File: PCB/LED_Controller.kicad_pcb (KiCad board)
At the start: 2 copper layers, 89.5 x 60.5 mm, 87 parts, among them J1 Barrel_Jack, J2 Conn_01x06_Female, J3 74984104400, J4 Screw_Terminal_01x02, J5 Screw_Terminal_01x04, Q1 MMBF170, U1 ESP32-PICO-D4, U2 AP62200WU-7, U3 TPS2372, U4 74LVCH2T45DC, U5 LAN8720A, U6 MCP1792x-5002xCB, U7 VCB4805SBO-50WR3, Y1 ECS-250-20-33-CKM-TR

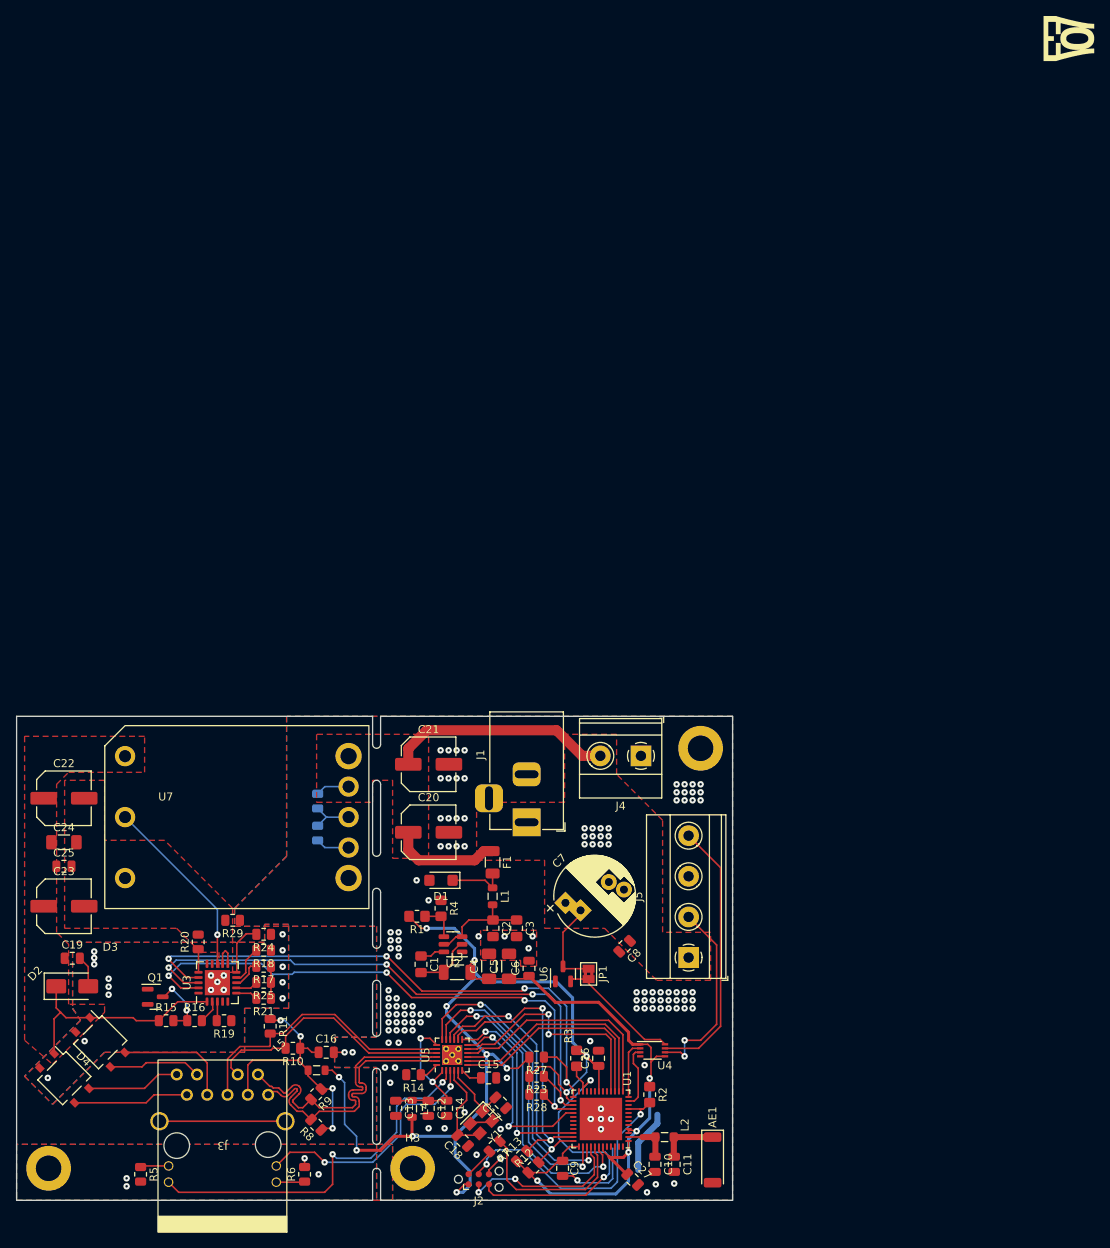
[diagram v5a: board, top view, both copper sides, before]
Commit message: Almost-Almost PCB design. Minor improvements on copper layer Silkscreen cleanup schematic sheet cleanup (now with subsheet titles)
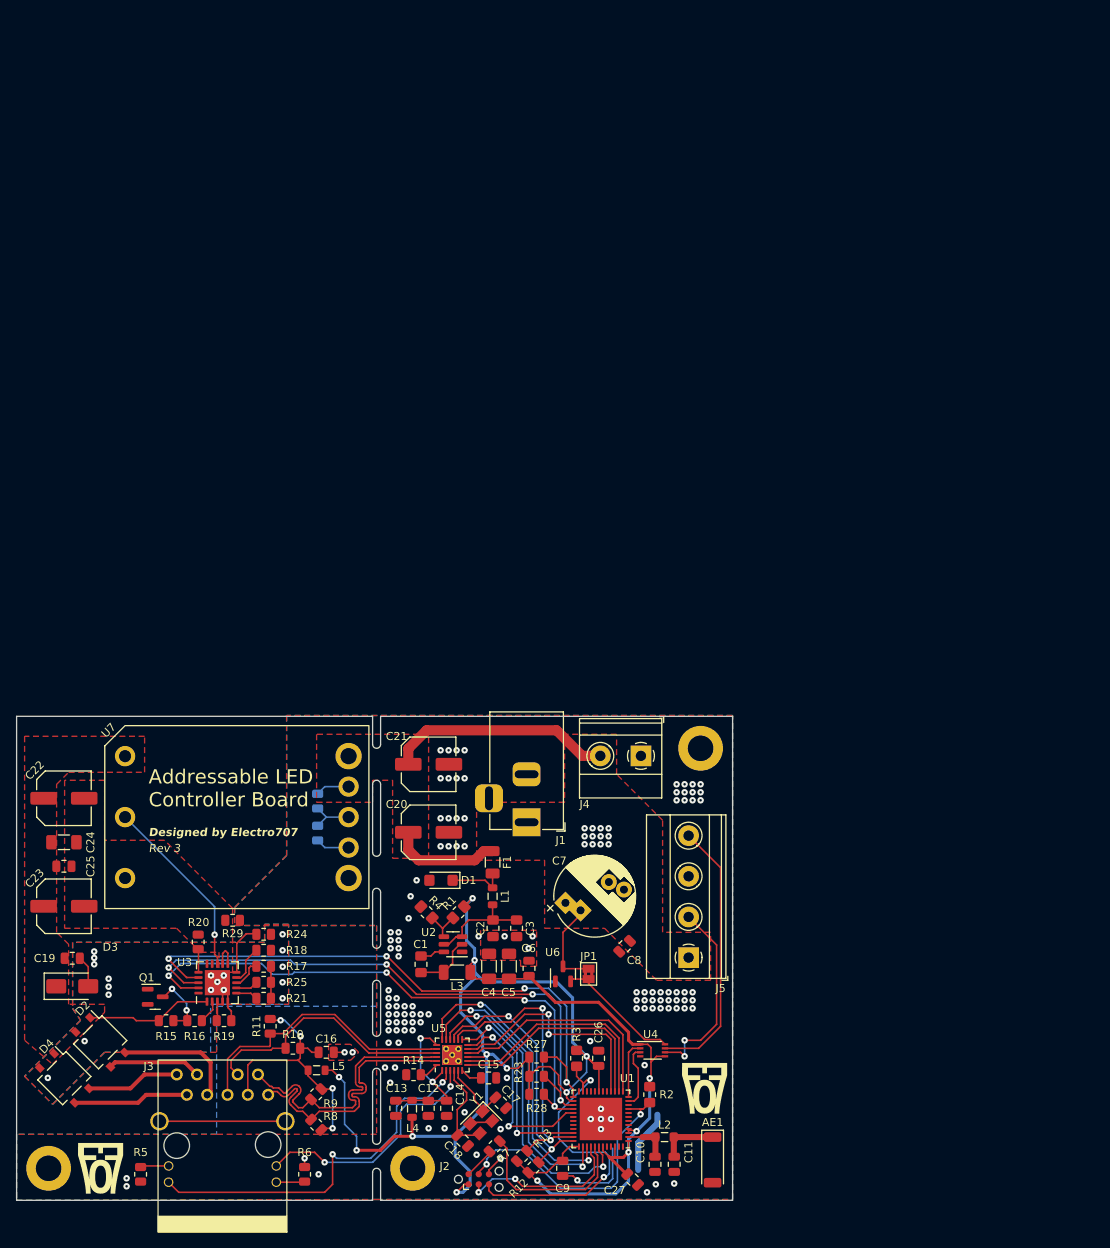
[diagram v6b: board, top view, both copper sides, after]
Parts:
- added G***: LOGO, LOGO, F.Cu at (134.5, 164.5)
- moved G*** 193.9 mm to (59.5, 174.5)
- moved G*** 186.0 mm to (59.0, 174.5), turned to 0 degrees
- moved R1 5.22 mm to (103.8, 142.5), turned to 45 degrees
- moved R4 1.87 mm to (99.8, 142.5), turned to -45 degrees
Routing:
- net Net-(D2-+): track 28.8 -> 15.8 mm
- net Net-(D2--): track 8.00 -> 13.8 mm
- net +3V3: track 228.5 -> 225.2 mm, vias 15 -> 14
- net /Ethernet and Connector/ETH_V1+: track 14.8 -> 15.5 mm
- net GND: vias 128 -> 129
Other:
- board text added: "Main Driver Side"
- board text added: "POE Side"

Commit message: Final Rev 3 board
Many changes that are finalization changes mostly
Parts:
- removed Q1: MMBF170, Package_TO_SOT_SMD:SOT-23
- added G***: LOGO, LOGO, B.Cu at (124.5, 147.0)
- added JP2: Jumper_2_Bridged, Connector_PinHeader_2.54mm:PinHeader_1x02_P2.54mm_Vertical, F.Cu at (64.0, 150.4)
- added R30: 0, Resistor_SMD:R_0805_2012Metric, F.Cu at (63.2, 169.7)
- added kibuzzard-64D45D66: G***, kibuzzard-64D45D66, F.Cu at (126.2, 130.3)
- added kibuzzard-64D45D6B: G***, kibuzzard-64D45D6B, F.Cu at (121.4, 130.3)
- added kibuzzard-64D45DB0: G***, kibuzzard-64D45DB0, F.Cu at (135.0, 152.1)
- added kibuzzard-64D45DB7: G***, kibuzzard-64D45DB7, F.Cu at (135.0, 153.7)
- added kibuzzard-64D45DBB: G***, kibuzzard-64D45DBB, F.Cu at (135.0, 155.2)
- added kibuzzard-64D45DC1: G***, kibuzzard-64D45DC1, F.Cu at (135.0, 156.7)
- added kibuzzard-64D45DDA: G***, kibuzzard-64D45DDA, F.Cu at (117.9, 122.9)
- C10, C11: footprint Capacitor_SMD:C_0805_2012Metric -> Capacitor_SMD:C_0603_1608Metric
- L2: footprint Inductor_SMD:L_0805_2012Metric_Pad1.05x1.20mm_HandSolder -> Inductor_SMD:L_0603_1608Metric
- U3: footprint Package_DFN_QFN:Texas_S-PVQFN-N20_EP3.15x3.15mm -> ProjectFootprints:TI_RGW0020B
- moved C10 0.96 mm to (128.8, 173.2)
- moved C11 0.88 mm to (130.4, 173.2)
- moved G*** 0.50 mm to (59.0, 174.5)
- moved L2 0.10 mm to (129.6, 170.6)
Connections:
- J3 pad SH: unconnected-(J3-PadSH) -> Net-(J3-PadSH)
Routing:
- net Net-(J3-PadSH): track 0.00 -> 18.9 mm
- net unconnected-(J3-PadSH): track 15.7 -> 0.00 mm
- net GND: track 30.7 -> 44.1 mm, vias 129 -> 128
- net +3V3: track 225.2 -> 231.2 mm
- net Net-(J3-CD): track 33.3 -> 38.2 mm
- net /Ethernet and Connector/ETH_TX+: track 34.3 -> 30.5 mm
- net /Ethernet and Connector/ETH_TX-: track 36.0 -> 32.3 mm
- net Net-(JP2-B): track 8.07 -> 10.8 mm
- net Net-(U1-LNA_IN): track 5.97 -> 5.31 mm
- net Vdda2: track 19.8 -> 19.3 mm
- net Net-(D2--): vias 18 -> 13

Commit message: Updated to Rev 4
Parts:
- removed C12, C13, C14, C15, C16: 1uF, Capacitor_SMD:C_0805_2012Metric
- removed C18: C, Capacitor_SMD:C_0805_2012Metric
- removed C19, C25: 0.1u, Capacitor_SMD:C_0805_2012Metric
- removed C20: 330uF, Capacitor_SMD:C_Elec_6.3x5.4
- removed C21: 0.1u, Capacitor_SMD:C_Elec_6.3x5.4
- removed C22: 100uF, Capacitor_SMD:C_Elec_6.3x5.4
- removed C23: 100uF, Capacitor_SMD:C_Elec_6.3x5.8
- removed C24: 1uF, Capacitor_SMD:C_1206_3216Metric_Pad1.33x1.80mm_HandSolder
- removed C4: 10uF, Capacitor_SMD:C_1206_3216Metric_Pad1.33x1.80mm_HandSolder
- removed C7: 1000uF, Capacitor_THT:CP_Radial_D10.0mm_P5.00mm_P7.50mm
- removed D3: SMAJ58A, Diode_SMD:D_SMA
- removed D4: CDBHM220L, Package_TO_SOT_SMD:TO-269AA
- removed G*** (x4): LOGO, LOGO
- removed H1, H2, H3: MountingHole_Pad, MountingHole:MountingHole_3.2mm_M3_DIN965_Pad
- removed J4: Screw_Terminal_01x02, TerminalBlock_Phoenix:TerminalBlock_Phoenix_MKDS-1,5-2-5.08_1x02_P5.08mm_Horizontal
- removed JP2: Jumper_2_Bridged, Connector_PinHeader_2.54mm:PinHeader_1x02_P2.54mm_Vertical
- removed L4, L5: L_Ferrite, Inductor_SMD:L_0805_2012Metric
- removed R10, R11, R8, R9: 49.9, Resistor_SMD:R_0805_2012Metric
- removed R12, R13, R23, R27, R28: 10k, Resistor_SMD:R_0805_2012Metric
- removed R14: 12.1k, Resistor_SMD:R_0805_2012Metric
- removed R15, R16, R17, R18, R19, R21, R22, R24, R25, R26: R, Resistor_SMD:R_0805_2012Metric
- removed R20, R29, R30: 0, Resistor_SMD:R_0805_2012Metric
- removed R5, R6: 1k, Resistor_SMD:R_0805_2012Metric
- removed U6: MCP1792x-5002xCB, Package_TO_SOT_SMD:SOT-23
- removed U7: VCB4805SBO-50WR3, ProjectFootprints:VCB4805SBO-50WR3
- removed Y1: ECS-250-20-33-CKM-TR, Crystal:Crystal_SMD_3225-4Pin_3.2x2.5mm
- removed kibuzzard-64D45D66: G***, kibuzzard-64D45D66
- removed kibuzzard-64D45D6B: G***, kibuzzard-64D45D6B
- removed kibuzzard-64D45DB0: G***, kibuzzard-64D45DB0
- removed kibuzzard-64D45DB7: G***, kibuzzard-64D45DB7
- removed kibuzzard-64D45DBB: G***, kibuzzard-64D45DBB
- removed kibuzzard-64D45DC1: G***, kibuzzard-64D45DC1
- removed kibuzzard-64D45DDA: G***, kibuzzard-64D45DDA
- added J6: Screw_Terminal_01x04, TerminalBlock_TE-Connectivity:TerminalBlock_TE_282834-4_1x04_P2.54mm_Horizontal, F.Cu at (69.1, 75.2)
- C1, C2: footprint Capacitor_SMD:C_0805_2012Metric_Pad1.18x1.45mm_HandSolder -> Capacitor_SMD:C_0603_1608Metric; moved to B.Cu
- C17: value C -> 0.1u; footprint Capacitor_SMD:C_0805_2012Metric -> Capacitor_SMD:C_0603_1608Metric; moved to B.Cu
- C26, C27, C9: footprint Capacitor_SMD:C_0805_2012Metric -> Capacitor_SMD:C_0603_1608Metric
- C3: value 10uF -> 22uF; footprint Capacitor_SMD:C_0805_2012Metric_Pad1.18x1.45mm_HandSolder -> Capacitor_SMD:C_1206_3216Metric_Pad1.33x1.80mm_HandSolder; moved to B.Cu
- C5, D1, F1, L1, L3, R1, R4, U2: moved to B.Cu
- C6, C8: footprint Capacitor_SMD:C_0805_2012Metric -> Capacitor_SMD:C_0603_1608Metric; moved to B.Cu
- D2: value CDBHM220L -> SP0505BAHT; footprint Package_TO_SOT_SMD:TO-269AA -> Package_TO_SOT_SMD:SOT-23-6; moved to B.Cu
- J3: value 74984104400 -> Screw_Terminal_01x02; footprint ProjectFootprints:74984104400 -> TerminalBlock_Phoenix:TerminalBlock_Phoenix_MKDS-1,5-2-5.08_1x02_P5.08mm_Horizontal
- J5: value Screw_Terminal_01x04 -> Screw_Terminal_01x02; footprint TerminalBlock_Phoenix:TerminalBlock_Phoenix_MKDS-1,5-4-5.08_1x04_P5.08mm_Horizontal -> TerminalBlock_Phoenix:TerminalBlock_Phoenix_PT-1,5-2-3.5-H_1x02_P3.50mm_Horizontal
- JP1: footprint Jumper:SolderJumper-2_P1.3mm_Bridged2Bar_Pad1.0x1.5mm -> Jumper:SolderJumper-2_P1.3mm_Open_TrianglePad1.0x1.5mm; moved to B.Cu
- R2: footprint Resistor_SMD:R_0805_2012Metric_Pad1.20x1.40mm_HandSolder -> Resistor_SMD:R_0603_1608Metric
- R3: footprint Resistor_SMD:R_0805_2012Metric_Pad1.20x1.40mm_HandSolder -> Resistor_SMD:R_0603_1608Metric; moved to B.Cu
- R7: footprint Resistor_SMD:R_0805_2012Metric -> Resistor_SMD:R_0603_1608Metric_Pad0.98x0.95mm_HandSolder
- U3: value TPS2372 -> 74LVCH2T45DC; footprint ProjectFootprints:TI_RGW0020B -> Package_SO:VSSOP-8_2.3x2mm_P0.5mm
- U5: value LAN8720A -> MCP1792x-5002xCB; footprint Package_DFN_QFN:VQFN-24-1EP_4x4mm_P0.5mm_EP2.5x2.5mm_ThermalVias -> Package_TO_SOT_SMD:SOT-23; moved to B.Cu
- moved AE1 122.9 mm to (69.5, 69.8), turned to 180 degrees
- moved C11 114.7 mm to (76.0, 72.2)
- moved L2 113.8 mm to (76.8, 69.8), turned to 180 degrees
- moved C10 113.2 mm to (77.7, 72.2)
- moved C27 109.9 mm to (83.7, 74.3), turned to 135 degrees
- moved J2 107.6 mm to (84.4, 70.6), turned to 180 degrees
- moved R2 102.4 mm to (77.5, 76.0), turned to -135 degrees
- moved R7 99.7 mm to (86.2, 74.5), turned to 90 degrees
- moved U1 97.0 mm to (81.6, 79.9), turned to -45 degrees
- moved C9 95.3 mm to (84.5, 84.8), turned to 45 degrees
- moved R3 91.9 mm to (76.5, 79.0), turned to 0 degrees
- moved J5 87.1 mm to (70.3, 87.2), turned to -90 degrees
- moved U4 86.5 mm to (79.2, 88.3), turned to 180 degrees
- moved C26 85.5 mm to (86.9, 82.4), turned to -135 degrees
- moved J3 85.4 mm to (97.5, 89.5), turned to 90 degrees
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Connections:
- C17 pad 1: GND -> +3V3
- C17 pad 2: Net-(U5-XTAL1/CLKIN) -> GND
- D2 pad 1: Net-(D2-+) -> /LED2-CLK_{H}
- D2 pad 2: Net-(D2--) -> GND
- D2 pad 3: /Ethernet and Connector/ETH_V1- -> /LED2-DATA_{H}
- D2 pad 4: /Ethernet and Connector/ETH_V1+ -> unconnected-(D2-K-Pad4)
- J2 pad 1: +3V3 -> /RX
- J2 pad 3: /RX -> +3V3
- J3 pad 1: /Ethernet and Connector/ETH_TX+ -> GND
- J3 pad 2: /Ethernet and Connector/ETH_TX- -> VIN
- J5 pad 1: VIN -> GND
- J5 pad 2: /LED1-DATA_{H} -> VIN
- U1 pad 11: /LED1-DATA_{L} -> unconnected-(U1-IO35-Pad11)
- U1 pad 12: /LED1-CLK_{L} -> unconnected-(U1-IO32-Pad12)
- U1 pad 13: /E_RXER -> unconnected-(U1-IO33-Pad13)
- U1 pad 14: /E_RXD0 -> unconnected-(U1-IO25-Pad14)
- U1 pad 15: /E_RXD1 -> unconnected-(U1-IO26-Pad15)
- U1 pad 16: /E_CRS -> unconnected-(U1-IO27-Pad16)
- U1 pad 17: unconnected-(U1-IO14-Pad17) -> /LED2-CLK_{L}
- U1 pad 18: unconnected-(U1-IO12-Pad18) -> /LED2-DATA_{L}
- U1 pad 20: unconnected-(U1-IO13-Pad20) -> /LED1-CLK_{L}
- U1 pad 21: unconnected-(U1-IO15-Pad21) -> /LED1-DATA_{L}
- U1 pad 25: /POE_TPH -> unconnected-(U1-IO16-Pad25)
- U1 pad 27: /POE_~{BT} -> unconnected-(U1-IO17-Pad27)
- U1 pad 28: /POE_TPL -> unconnected-(U1-SD2/IO9-Pad28)
- U1 pad 29: /E_MDIO -> unconnected-(U1-SD3/IO10-Pad29)
- U1 pad 34: /E_MDC -> unconnected-(U1-IO5-Pad34)
- U1 pad 35: /E_~{INT} -> unconnected-(U1-IO18-Pad35)
- U1 pad 36: /E_~{RST} -> unconnected-(U1-IO23-Pad36)
- U1 pad 38: /E_TXD0 -> unconnected-(U1-IO19-Pad38)
- U1 pad 39: /E_TXD1 -> unconnected-(U1-IO22-Pad39)
- U1 pad 42: /E_TXEN -> unconnected-(U1-IO21-Pad42)
- U3 pad 1: Net-(D2-+) -> +3V3
- U3 pad 2: Net-(U3-DEN) -> /LED2-CLK_{L}
- U3 pad 3: Net-(U3-CLSA) -> /LED2-DATA_{L}
- U3 pad 4: Net-(D2--) -> GND
- U3 pad 5: Net-(D2--) -> +3V3
- U3 pad 6: Net-(U3-CLSB) -> /LED2-DATA_{H}
- U3 pad 7: Net-(U3-REF) -> /LED2-CLK_{H}
- U3 pad 8: Net-(U3-AMPS_CTL) -> +5V
- U5 pad 1: Vdda2 -> GND
- U5 pad 2: /Ethernet and Connector/ETH_LED2 -> +5V
- U5 pad 3: /Ethernet and Connector/ETH_LED1 -> VIN
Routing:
- net +3V3: track 231.2 -> 55.3 mm, vias 14 -> 11
- net /POE_TPH: track 74.7 -> 0.00 mm, vias 4 -> 0
- net /POE_~{BT}: track 74.0 -> 0.00 mm, vias 4 -> 0
- net /POE_TPL: track 72.6 -> 0.00 mm, vias 4 -> 0
- net /Ethernet and Connector/ETH_LED2: track 46.9 -> 0.00 mm, vias 2 -> 0
- net /E_TXEN: track 38.7 -> 0.00 mm, vias 2 -> 0
- net Net-(J3-CD): track 38.2 -> 0.00 mm, vias 4 -> 0
- net /E_TXD1: track 37.8 -> 0.00 mm, vias 2 -> 0
- net /E_TXD0: track 36.7 -> 0.00 mm, vias 2 -> 0
- net /E_~{INT}: track 35.9 -> 0.00 mm, vias 2 -> 0
- net /Ethernet and Connector/ETH_RX-: track 35.3 -> 0.00 mm
- net /E_~{RST}: track 32.7 -> 0.00 mm, vias 2 -> 0
- net /Ethernet and Connector/ETH_TX-: track 32.3 -> 0.00 mm
- net /Ethernet and Connector/ETH_RX+: track 32.3 -> 0.00 mm
- net /Ethernet and Connector/ETH_LED1: track 31.0 -> 0.00 mm, vias 2 -> 0
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- added copper zone on B.Cu, net +3V3
- added copper zone on In2.Cu, net +3V3
- added copper zone on In1.Cu, net GND
- removed copper zone on F.Cu, net Net-(D2-+)
- removed copper zone on B.Cu, net Net-(D2--)
- removed copper zone on F.Cu, net Net-(D2--)
- removed copper zone on F.Cu, net Net-(U7-GND)
- removed copper zone on F.Cu, net VIN
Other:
- board size 89.5 x 60.5 mm -> 37.8 x 25 mm
- copper layers 2 -> 4
- board text added: "+"
- board text added: "-"
- board text added: "IO12"
- board text added: "IO12 IO14 IO15 IO13"
- board text added: "IO13"
- board text added: "IO14"
- board text added: "IO15"
- board text added: "Rev 4"
- board text added: "Tiny LED Driver"
- board text removed: "Addressable LED Controller Board"
- board text removed: "Main Driver Side"
- board text removed: "POE Side"
- board text removed: "Rev 3"
